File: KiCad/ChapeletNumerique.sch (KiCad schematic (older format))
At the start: 24 parts

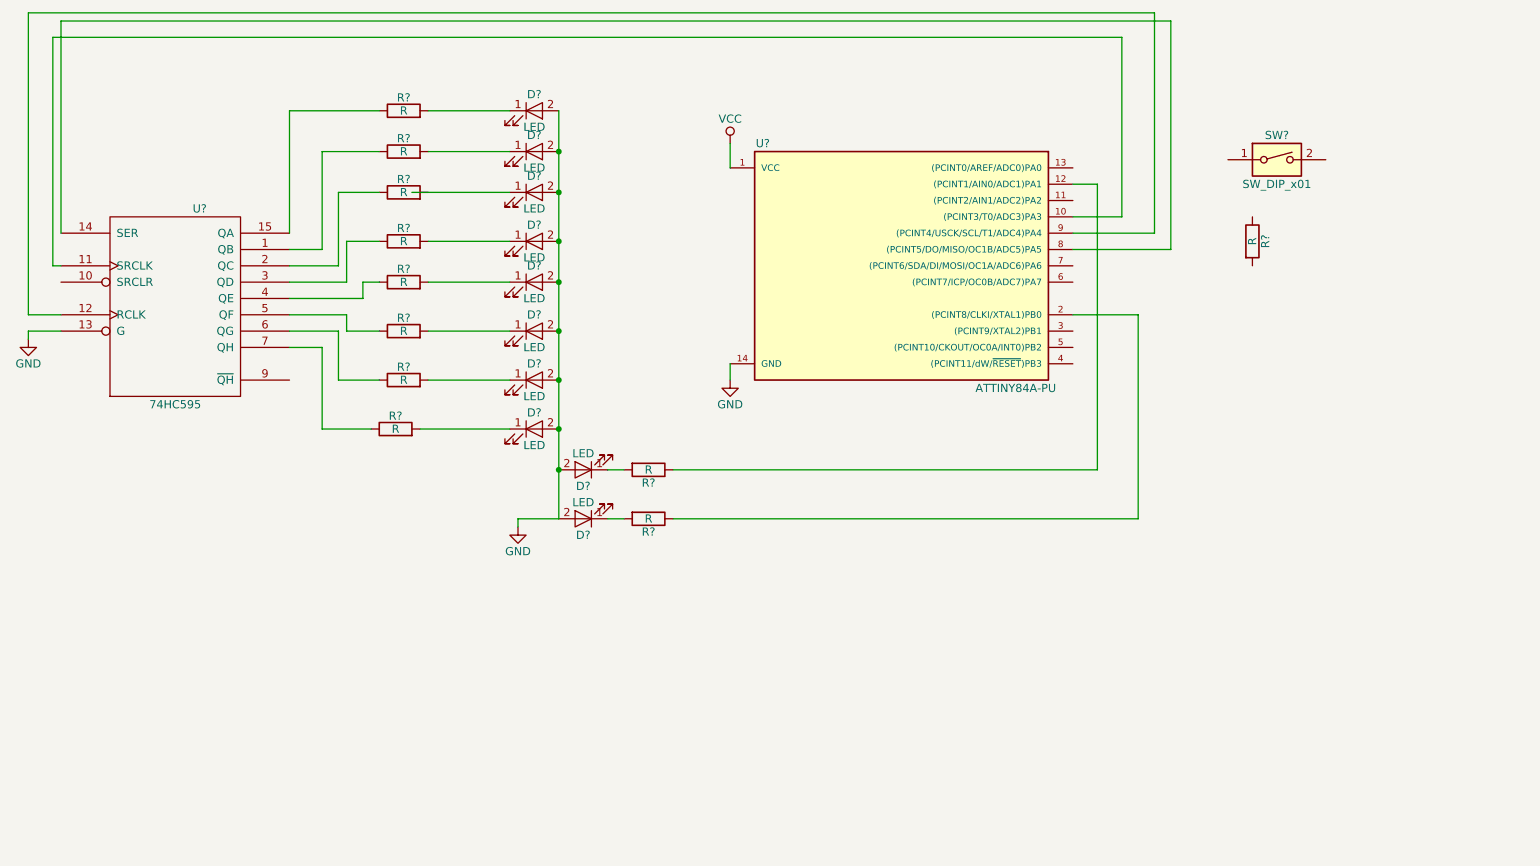
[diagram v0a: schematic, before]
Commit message: feat(KiCad) finish schematics
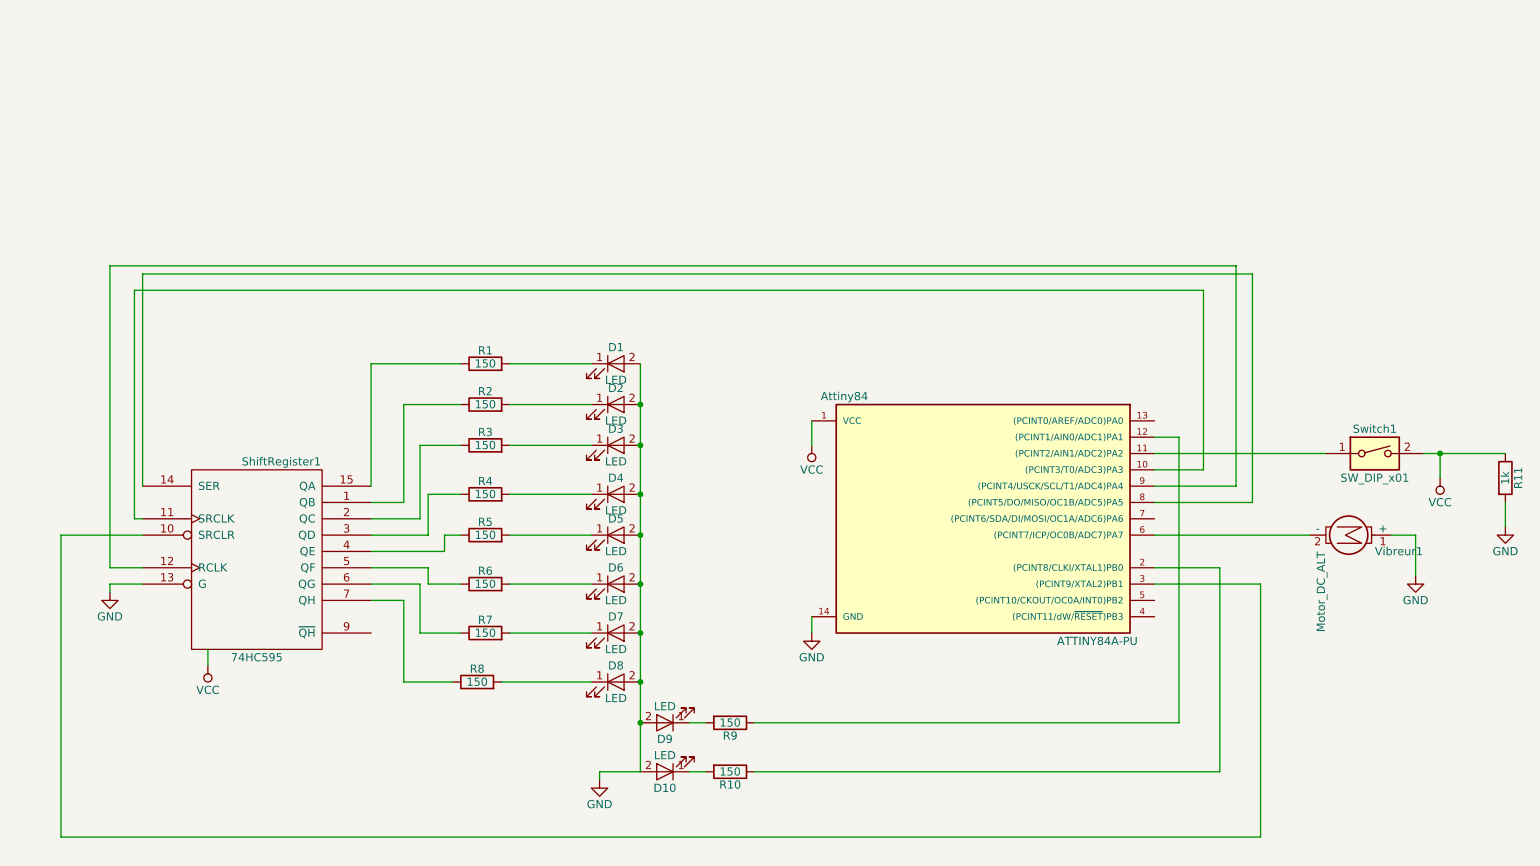
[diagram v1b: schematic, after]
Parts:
- added Vibreur1: Motor_DC_ALT, symbol Motor_DC_ALT
- R1, R10, R2, R3, R4, R5, R6, R7, R8, R9: renamed from R?; value R -> 150
- R11: renamed from R?; value R -> 1k
- gave numbers to parts that had none: 13
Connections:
- net VCC is gone; now on net GND: Attiny84.1 (VCC), ShiftRegister1.16 (VCC)
- net GND: now also R11.1, R11.2, Switch1.2, Vibreur1.1 (+)
- net at R3.2: now also D3.1 (K)
- net at Attiny84.11 ((PCINT2/AIN1/ADC2)PA2): now also Switch1.1
- net at Attiny84.3 ((PCINT9/XTAL2)PB1): now also ShiftRegister1.10 (SRCLR)
- net at Attiny84.6 ((PCINT7/ICP/OC0B/ADC7)PA7): now also Vibreur1.2 (-)
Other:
- moved on the sheet: Attiny84, D1, D10, D2, D3, D4, D5, D6, D7, D8, D9, R1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

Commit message: feat(kicad) update schematic
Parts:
- added A1: Alimentation, Pin_Headers:Pin_Header_Angled_1x02_Pitch1.27mm, symbol Conn_01x02
- D1, D10, D2, D3, D4, D5, D6, D7, D8, D9: footprint (none) -> LEDs:LED_D3.0mm
- R1, R10, R11, R2, R3, R4, R5, R6, R7, R8, R9: footprint (none) -> Resistors_THT:R_Axial_DIN0204_L3.6mm_D1.6mm_P7.62mm_Horizontal
- ShiftRegister1: footprint (none) -> Housings_DIP:DIP-16_W7.62mm_Socket
- Switch1: footprint (none) -> Buttons_Switches_SMD:SW_DIP_x1_W7.62mm_Slide_Copal_CHS-B
- Vibreur1: footprint (none) -> TerminalBlocks_Phoenix:TerminalBlock_Phoenix_MPT-2.54mm_2pol
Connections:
- net GND: now also A1.1 (Pin_1); no longer Attiny84.1 (VCC), R11.1, ShiftRegister1.16 (VCC), Switch1.2
- net switch: now reaches Attiny84.11 ((PCINT2/AIN1/ADC2)PA2), Switch1.1
- new net VCC: A1.2 (Pin_2), Attiny84.1 (VCC), R11.1, ShiftRegister1.16 (VCC), Switch1.2
- no-connect marks 0 -> 5
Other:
- moved on the sheet: Attiny84, D1, D10, D2, D3, D4, D5, D6, D7, D8, D9, R1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
